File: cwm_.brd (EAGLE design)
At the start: 49.2 x 41.9 mm, 71 parts, among them U1 STM32L476, U2 24AA64T, U3 LSM9DS0, U4 MS5803-14BA, U5 MX25L25635F, U6 RN4020, U7 LTR-303ALS, U8 LM393, X1 EPSON FA-128 24.0000MF10Z-W3, X2 ABS06-32.768KHZ-9-1-T

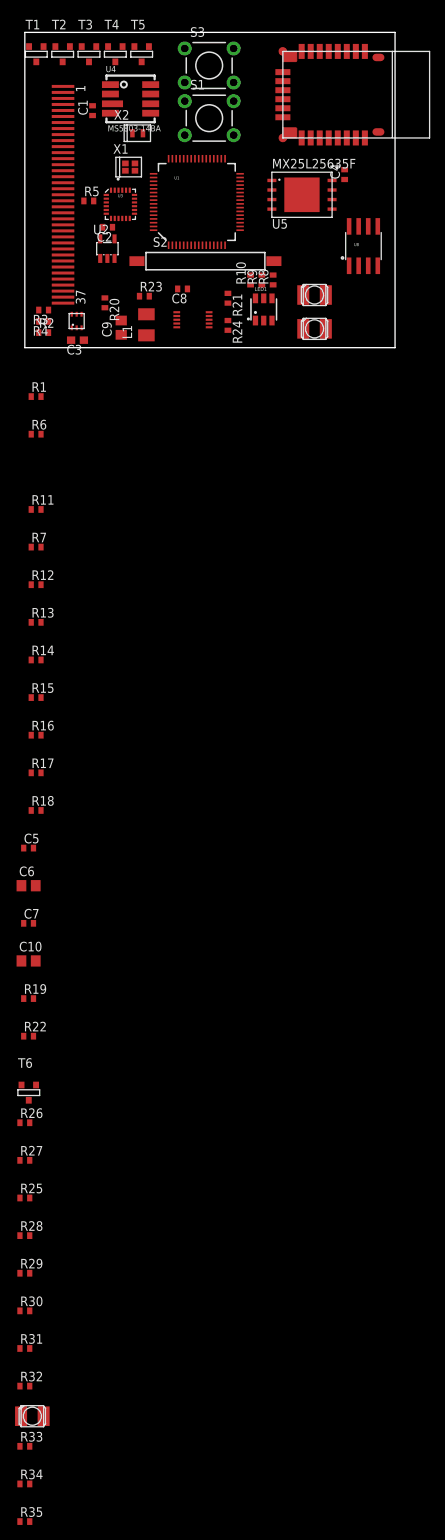
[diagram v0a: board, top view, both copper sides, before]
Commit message: added all UCs
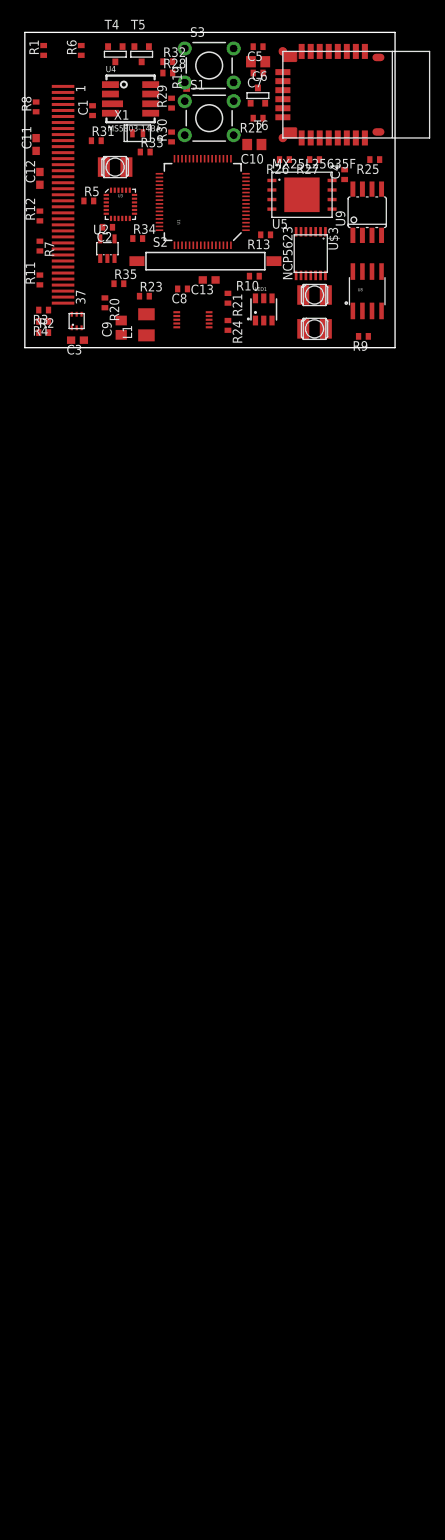
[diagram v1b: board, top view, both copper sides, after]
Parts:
- removed R14, R16, R18: 100k, resistor:R0402
- removed R15, R17: 100R, resistor:R0402
- removed T1, T2, T3: (no value), zetex:SOT-23
- removed X2: ABS06-32.768KHZ-9-1-T, IQD-Frequency-Products:2.0X1.2-2PAD
- added C11, C12: 1uF, resistor:C0603
- added C13: 10nF, resistor:C0603
- added U$3: NCP5623, NCP5623:NCP5623
- added U9: MK3200, MK3200:SOIC8
- R10: value 5R -> 100k
- R13: value 100R -> 100k
- R8: value 5R -> 62k
- R9: value 60R -> 33R
- X1: value EPSON FA-128 24.0000MF10Z-W3 -> ABS06-32.768KHZ-9-1-T; device IQD-Frequency-Products:2.0X1.6-4-PAD -> IQD-Frequency-Products:2.0X1.2-2PAD
- moved R32 177.0 mm to (19.0, 38.0)
- moved R33 172.7 mm to (16.0, 26.0)
- moved PT3 166.4 mm to (12.0, 24.0)
- moved R34 166.2 mm to (15.0, 14.5)
- moved R35 165.0 mm to (12.5, 8.50)
- moved R31 160.8 mm to (9.50, 27.5)
- moved R30 157.2 mm to (19.5, 28.0), turned to 90 degrees
- moved R29 156.7 mm to (19.5, 32.5), turned to 90 degrees
- moved R28 155.7 mm to (19.0, 36.5)
- moved R25 145.6 mm to (46.5, 25.0), turned to 180 degrees
- moved R27 138.5 mm to (38.5, 25.0), turned to 180 degrees
- moved T6 136.0 mm to (31.0, 33.5), turned to 180 degrees
- moved R26 132.6 mm to (34.5, 25.0), turned to 180 degrees
- moved R22 125.8 mm to (31.0, 30.5), turned to 180 degrees
- moved R19 123.3 mm to (21.5, 35.0), turned to 90 degrees
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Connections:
- removed net N$26: R17.1, R18.1, T1.3
- removed net N$27: R17.2
- net GND: now also C11.1, C12.2, C13.1, R8.2, S1.3, S3.3, U$3.2, U$3.6, U9.3, U9.6, U9.7; no longer R14.2, R16.2, R18.2, T1.2, T2.2, T3.2
- net N$11: now also U$3.4; no longer T1.1
- net N$12: now also LED1.CB, U$3.3; no longer LED1.CR, T2.1
- net N$13: now also LED1.CR, U$3.5; no longer LED1.CB, T3.1
- net N$19: now also U9.1, X1.2; no longer R13.1, R14.1, T2.3
- net N$20: now also U$3.10; no longer LED1.AG
- net N$21: now also U9.8, X1.1; no longer LED1.AR, R9.1
- net N$22: now also R9.1, U9.4; no longer LED1.AB, R10.1
- net N$23: now also U$1.10; no longer R13.2
- net N$24: now also R10.2, S1.1; no longer R15.1, R16.1, T3.3
- net N$25: now also R13.1, S3.1; no longer R15.2
- net SCL: now also U$3.11
- net SDA: now also U$3.9
- net VCC: now also C13.2, R10.1, R13.2, U9.2, U9.5; no longer R10.2, R8.2, R9.2, U$1.10
- net VIN: now also C11.2, C12.1, LED1.AB, LED1.AG, LED1.AR, U$3.12, U$3.13

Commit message: some changes
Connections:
- removed net GND1: U6.1
- removed net GND2: U6.9
- removed net GND3: U6.16
- new net N$26: R9.2, U1.3
- new net N$27: U6.6
- new net N$43: U6.5
- new net N$44: U6.18
- new net N$45: U6.14
- new net N$46: U6.8
- new net N$47: U6.7
- new net N$48: U6.15
- new net N$49: U6.10
- new net N$50: U6.11
- new net N$51: U6.12
- new net N$53: U5.1
- new net N$54: U5.2
- new net N$55: U5.7
- new net N$56: U5.6
- new net N$57: U5.5
- net GND: now also U1.31, U1.47, U6.1, U6.16, U6.9
- net N$23: now also U1.6
- net N$39: now also U1.4
- net N$5: now also U1.2
- net N$7: now also U1.5
- net SCL: now also U1.8
- net SDA: now also U1.9
- net VCC: now also U6.23
- net VDD: no longer U6.23

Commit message: everything commected (draftely)
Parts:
- added R14, R15: 60k, resistor:R0402
- C6: value 4.7uF - ceramic -> 4.7uF
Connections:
- removed net N$35: R22.2, U3.13
- removed net N$36: R19.2, U3.12
- removed net N$48: U6.15
- new net DRDY_G: R19.2, U1.54, U3.12
- new net INT1_XM: R22.2, U1.53, U3.13
- new net INT_LTR: R4.2, U1.10, U7.5
- new net N$60: R14.2, R15.1, U1.11
- net GND: now also R14.1
- net N$16: now also U1.14
- net N$18: now also U1.15
- net N$23: now also U1.49; no longer U1.6
- net N$24: now also U1.2
- net N$25: now also U1.25
- net N$27: now also U1.42
- net N$41: now also U1.38
- net N$42: now also U1.39
- net N$43: now also U1.43
- net N$44: now also U1.44
- net N$45: now also U1.45
- net N$46: now also U1.40
- net N$47: now also U1.41
- net N$49: now also U1.52
- net N$5: now also U1.6, U6.15; no longer R35.1, U$9.2, U1.2
- net N$50: now also U1.51
- net N$51: now also U1.50
- net N$53: now also U1.20
- net N$54: now also U1.22
- net N$55: now also U1.37
- net N$56: now also U1.21
- net N$57: now also U1.23
- net N$6: now also U1.17
- net N$8: now also U1.16
- net N$9: now also R35.1, U$9.2, U1.24; no longer R4.2, U7.5
- net VIN: now also R15.2
